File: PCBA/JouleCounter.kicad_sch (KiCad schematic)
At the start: 1 part, among them J101 JTAG

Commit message: Rough outline
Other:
- sheet Main MCU ports: added ~{RESET}; removed none
- sheet UI ports: added INT, SCL, SDA, ~{LCD Reset}; removed none

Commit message: More rough placement
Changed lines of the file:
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@@
+    (effects (font (size 1.27 1.27)) (justify left bottom))
+  )
+  (label "SENSE_USB_D+" (at 76.2 71.12 0)
     (effects (font (size 1.27 1.27)) (justify left bottom))
   )
@@
     (effects (font (size 1.27 1.27)) (justify left bottom))
   )
-  (label "VBus ADC" (at 76.2 93.98 0)
+  (label "VBus ADC" (at 76.2 91.44 0)
     (effects (font (size 1.27 1.27)) (justify left bottom))
   )
@@
     (effects (font (size 1.27 1.27)) (justify left bottom))
   )
+  (label "SENSE_USB_D-" (at 76.2 86.36 0)
+    (effects (font (size 1.27 1.27)) (justify left bottom))
+  )
   (label "I Sense 2" (at 254 69.85 180)
     (effects (font (size 1.27 1.27)) (justify right bottom))
@@
     (effects (font (size 1.27 1.27)) (justify left bottom))
   )
-  (label "USB D- DAC{slash}ADC" (at 76.2 86.36 0)
-    (effects (font (size 1.27 1.27)) (justify left bottom))
-  )
   (label "Spare GPIO 1" (at 76.2 96.52 0)
     (effects (font (size 1.27 1.27)) (justify left bottom))
@@
     (effects (font (size 1.27 1.27)) (justify left bottom))
   )
-  (label "USB D- DAC{slash}ADC" (at 76.2 88.9 0)
-    (effects (font (size 1.27 1.27)) (justify left bottom))
-  )
   (label "JTAG TDO" (at 76.2 121.92 0)
     (effects (font (size 1.27 1.27)) (justify left bottom))
   )
-  (label "Current ADC" (at 76.2 91.44 0)
+  (label "Current ADC" (at 76.2 93.98 0)
     (effects (font (size 1.27 1.27)) (justify left bottom))
   )
@@
     (effects (font (size 1.27 1.27)) (justify left bottom))
   )
-  (label "SENSE_USB_D-" (at 76.2 73.66 0)
+  (label "SENSE_USB_D-" (at 76.2 88.9 0)
     (effects (font (size 1.27 1.27)) (justify left bottom))
   )
@@
     (effects (font (size 1.27 1.27)) (justify left bottom))
   )
-  (label "SENSE_USB_D+" (at 76.2 71.12 0)
-    (effects (font (size 1.27 1.27)) (justify left bottom))
-  )
   (label "Uart Rx" (at 254 116.84 180)
     (effects (font (size 1.27 1.27)) (justify right bottom))
@@
   )
   (label "JTAG TDI" (at 69.85 186.69 0)
+    (effects (font (size 1.27 1.27)) (justify left bottom))
+  )
+  (label "SENSE_USB_D+" (at 76.2 73.66 0)
     (effects (font (size 1.27 1.27)) (justify left bottom))
   )
@@
     )
     (path "/4847c8c0-6173-45c5-9b4b-8c9418cb5a91/3110ff89-db45-4c2b-ae20-9f45ed5b62f3"
-      (reference "L201") (unit 1) (value "2.2uH") (footprint "Inductor_SMD:L_Wuerth_MAPI-3010")
+      (reference "L201") (unit 1) (value "2.2uH") (footprint "Inductor_SMD:L_0805_2012Metric")
     )
     (path "/3f787304-0f09-428f-9615-a178d53b5ed2/eecc54f1-353d-4bbc-bb3a-293df7de7d03/d1c7fa2b-6f66-447f-ab0d-f943727d6017"

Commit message: Routing
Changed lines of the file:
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@@
     (effects (font (size 1.27 1.27)) (justify left bottom))
   )
-  (label "Spare GPIO 1" (at 76.2 96.52 0)
+  (label "Spare GPIO 1" (at 76.2 119.38 0)
     (effects (font (size 1.27 1.27)) (justify left bottom))
   )
@@
     (effects (font (size 1.27 1.27)) (justify right bottom))
   )
-  (label "LCD DC" (at 76.2 109.22 0)
+  (label "LCD DC" (at 76.2 96.52 0)
     (effects (font (size 1.27 1.27)) (justify left bottom))
   )
@@
     (effects (font (size 1.27 1.27)) (justify left bottom))
   )
-  (label "~{TOUCH_IRQ}" (at 76.2 119.38 0)
+  (label "~{TOUCH_IRQ}" (at 76.2 109.22 0)
     (effects (font (size 1.27 1.27)) (justify left bottom))
   )
@@
       (reference "C909") (unit 1) (value "0.1u") (footprint "Capacitor_SMD:C_0603_1608Metric")
     )
-    (path "/61f092db-d732-44e6-ab5b-e56a273f9e01/f833cedb-fa6c-45d4-8bc9-06cb22231f00"
-      (reference "C910") (unit 1) (value "0.1u") (footprint "Capacitor_SMD:C_0603_1608Metric")
-    )
     (path "/61f092db-d732-44e6-ab5b-e56a273f9e01/861d8f10-f76f-4f14-9f74-e11cce68fcd9"
       (reference "C911") (unit 1) (value "1uf") (footprint "Capacitor_SMD:C_0603_1608Metric")
@@
     )
     (path "/3f787304-0f09-428f-9615-a178d53b5ed2/8a06555e-37b5-4e52-aed5-4db5d56c9572/01a2bdc6-039f-41f7-b045-94d753ea8bb9"
-      (reference "L1001") (unit 1) (value "47uH") (footprint "Inductor_SMD:L_Taiyo-Yuden_NR-40xx_HandSoldering")
+      (reference "L1001") (unit 1) (value "47uH") (footprint "Inductor_SMD:L_1210_3225Metric")
     )
     (path "/61f092db-d732-44e6-ab5b-e56a273f9e01/3dcb82af-5522-4234-9097-cffd473db105"

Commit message: molex model
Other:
- sheet ADC Measurements ports: added SCL, SDA, Vsense+, Vsense-, ~{ALERT}; removed ADC Current, ADC VBus, I Sense 1, I Sense 2, VBus In
- note added: "These are doubled up for ADC + DAC operation"
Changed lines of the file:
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@@
   (junction (at 57.15 186.69) (diameter 0) (color 0 0 0 0)
+  )
+  (polyline (pts (xy 88.9 83.82) (xy 91.44 83.82))
+    (stroke (width 0) (type default) (color 0 0 0 0))
   )
   (polyline (pts (xy 228.6 12.7) (xy 228.6 166.37))
@@
     (stroke (width 0) (type default) (color 0 0 0 0))
   )
+  (polyline (pts (xy 88.9 88.9) (xy 91.44 88.9))
+    (stroke (width 0) (type default) (color 0 0 0 0))
+  )
   (wire (pts (xy 57.15 181.61) (xy 57.15 184.15))
     (stroke (width 0) (type default) (color 0 0 0 0))
@@
     (stroke (width 0) (type default) (color 0 0 0 0))
   )
+  (polyline (pts (xy 91.44 68.58) (xy 91.44 73.66))
+    (stroke (width 0) (type default) (color 0 0 0 0))
+  )
   (wire (pts (xy 57.15 186.69) (xy 57.15 189.23))
     (stroke (width 0) (type default) (color 0 0 0 0))
   )
+  (polyline (pts (xy 88.9 68.58) (xy 91.44 68.58))
+    (stroke (width 0) (type default) (color 0 0 0 0))
+  )
+  (polyline (pts (xy 91.44 73.66) (xy 96.52 73.66))
+    (stroke (width 0) (type default) (color 0 0 0 0))
+  )
+  (polyline (pts (xy 88.9 73.66) (xy 91.44 73.66))
+    (stroke (width 0) (type default) (color 0 0 0 0))
+  )
+  (polyline (pts (xy 91.44 83.82) (xy 91.44 88.9))
+    (stroke (width 0) (type default) (color 0 0 0 0))
+  )
   (wire (pts (xy 57.15 184.15) (xy 57.15 186.69))
     (stroke (width 0) (type default) (color 0 0 0 0))
   )
+  (polyline (pts (xy 96.52 83.82) (xy 96.52 73.66))
+    (stroke (width 0) (type default) (color 0 0 0 0))
+  )
   (polyline (pts (xy 171.45 166.37) (xy 176.53 166.37))
+    (stroke (width 0) (type default) (color 0 0 0 0))
+  )
+  (polyline (pts (xy 91.44 83.82) (xy 96.52 83.82))
     (stroke (width 0) (type default) (color 0 0 0 0))
   )
@@
     (effects (font (size 1.27 1.27)) (justify left bottom))
   )
+  (text "These are doubled up for ADC + DAC operation" (at 97.79 77.47 0)
+    (effects (font (size 1.27 1.27)) (justify left bottom))
+  )
   (text "User Interface" (at 185.42 114.3 0)
     (effects (font (size 3 3)) (justify left bottom))
@@
     (effects (font (size 1.27 1.27)) (justify right bottom))
   )
-  (label "Spare GPIO 0" (at 76.2 83.82 0)
+  (label "Spare GPIO 0" (at 76.2 93.98 0)
     (effects (font (size 1.27 1.27)) (justify left bottom))
   )
@@
     (effects (font (size 1.27 1.27)) (justify left bottom))
   )
+  (label "5V_USB" (at 213.36 58.42 0)
+    (effects (font (size 1.27 1.27)) (justify left bottom))
+  )
   (label "~{Reset}" (at 76.2 34.29 0)
     (effects (font (size 1.27 1.27)) (justify left bottom))
@@
     (effects (font (size 1.27 1.27)) (justify right bottom))
   )
+  (label "~{ADC IRQ}" (at 76.2 91.44 0)
+    (effects (font (size 1.27 1.27)) (justify left bottom))
+  )
   (label "LCD SCK" (at 76.2 101.6 0)
     (effects (font (size 1.27 1.27)) (justify left bottom))
@@
     (effects (font (size 1.27 1.27)) (justify left bottom))
   )
-  (label "VBus ADC" (at 76.2 91.44 0)
-    (effects (font (size 1.27 1.27)) (justify left bottom))
-  )
-  (label "VBus" (at 215.9 78.74 0)
-    (effects (font (size 1.27 1.27)) (justify left bottom))
-  )
   (label "JTAG TDI" (at 76.2 45.72 0)
     (effects (font (size 1.27 1.27)) (justify left bottom))
@@
     (effects (font (size 1.27 1.27)) (justify left bottom))
   )
+  (label "~{ADC IRQ}" (at 190.5 83.82 180)
+    (effects (font (size 1.27 1.27)) (justify right bottom))
+  )
   (label "SENSE_USB_D+" (at 254 83.82 180)
     (effects (font (size 1.27 1.27)) (justify right bottom))
@@
     (effects (font (size 1.27 1.27)) (justify left bottom))
   )
+  (label "SDA" (at 190.5 78.74 180)
+    (effects (font (size 1.27 1.27)) (justify right bottom))
+  )
   (label "JTAG TCK" (at 69.85 181.61 0)
     (effects (font (size 1.27 1.27)) (justify left bottom))
@@
     (effects (font (size 1.27 1.27)) (justify left bottom))
   )
-  (label "Current ADC" (at 76.2 93.98 0)
-    (effects (font (size 1.27 1.27)) (justify left bottom))
-  )
   (label "~{TOUCH_IRQ}" (at 76.2 109.22 0)
     (effects (font (size 1.27 1.27)) (justify left bottom))
@@
     (effects (font (size 1.27 1.27)) (justify right bottom))
   )
+  (label "SCL" (at 190.5 81.28 180)
+    (effects (font (size 1.27 1.27)) (justify right bottom))
+  )
   (label "SCL" (at 76.2 78.74 0)
     (effects (font (size 1.27 1.27)) (justify left bottom))
   )
+  (label "5V_USB" (at 213.36 36.83 0)
+    (effects (font (size 1.27 1.27)) (justify left bottom))
+  )
   (label "SDA" (at 215.9 142.24 0)
     (effects (font (size 1.27 1.27)) (justify left bottom))
   )
-  (label "VBus ADC" (at 190.5 78.74 180)
-    (effects (font (size 1.27 1.27)) (justify right bottom))
-  )
   (label "CC2_X" (at 213.36 54.61 0)
     (effects (font (size 1.27 1.27)) (justify left bottom))
@@
   )
   (label "SDA" (at 254 119.38 180)
-    (effects (font (size 1.27 1.27)) (justify right bottom))
-  )
-  (label "Current ADC" (at 190.5 85.09 180)
     (effects (font (size 1.27 1.27)) (justify right bottom))
   )
@@
       (effects (font (size 1.27 1.27)) (justify left top))
     )
-    (pin "VBus In" input (at 215.9 78.74 0)
-      (effects (font (size 1.27 1.27)) (justify right))
-    )
-    (pin "I Sense 1" input (at 215.9 81.28 0)
-      (effects (font (size 1.27 1.27)) (justify right))
-    )
-    (pin "I Sense 2" input (at 215.9 83.82 0)
-      (effects (font (size 1.27 1.27)) (justify right))
-    )
-    (pin "ADC VBus" input (at 190.5 78.74 180)
-      (effects (font (size 1.27 1.27)) (justify left))
-    )
-    (pin "ADC Current" input (at 190.5 85.09 180)
+    (pin "SDA" input (at 190.5 78.74 180)
+      (effects (font (size 1.27 1.27)) (justify left))
+    )
+    (pin "SCL" input (at 190.5 81.28 180)
+      (effects (font (size 1.27 1.27)) (justify left))
+    )
+    (pin "Vsense+" input (at 215.9 81.28 0)
+      (effects (font (size 1.27 1.27)) (justify right))
+    )
+    (pin "Vsense-" input (at 215.9 83.82 0)
+      (effects (font (size 1.27 1.27)) (justify right))
+    )
+    (pin "~{ALERT}" input (at 190.5 83.82 180)
       (effects (font (size 1.27 1.27)) (justify left))
     )
@@
       (reference "#PWR0133") (unit 1) (value "GND") (footprint "")
     )
+    (path "/22f53838-7224-4d50-99f8-44746cd87af7/70cfc3de-356f-422f-8660-4b73d4360b3f"
+      (reference "#PWR0134") (unit 1) (value "VDD") (footprint "")
+    )
+    (path "/22f53838-7224-4d50-99f8-44746cd87af7/49693641-4499-473f-b005-4324d8fa543f"
+      (reference "#PWR0135") (unit 1) (value "GND") (footprint "")
+    )
     (path "/b0bcfef4-b206-452e-922a-e4174969def9/42d40598-f1c5-4992-939b-06617e7a59a8"
       (reference "#PWR0136") (unit 1) (value "GND") (footprint "")
@@
       (reference "#PWR0138") (unit 1) (value "GND") (footprint "")
     )
-    (path "/22f53838-7224-4d50-99f8-44746cd87af7/6a14883c-e23a-4bd5-84e9-8efebed799c9"
-      (reference "#PWR0139") (unit 1) (value "GND") (footprint "")
-    )
-    (path "/22f53838-7224-4d50-99f8-44746cd87af7/2116ac8a-6c19-4db6-aec1-63bf7b161e34"
-      (reference "#PWR0140") (unit 1) (value "VDD") (footprint "")
-    )
-    (path "/22f53838-7224-4d50-99f8-44746cd87af7/63d18546-978a-4ade-b5df-12f3cfd04a15"
-      (reference "#PWR0141") (unit 1) (value "GND") (footprint "")
-    )
-    (path "/22f53838-7224-4d50-99f8-44746cd87af7/c78b9413-d043-4274-8cdb-66dcb9cc5a63"
-      (reference "#PWR0142") (unit 1) (value "VDD") (footprint "")
-    )
-    (path "/22f53838-7224-4d50-99f8-44746cd87af7/0d93a723-51a6-484f-9d01-65584e9aaa36"
-      (reference "#PWR0143") (unit 1) (value "GND") (footprint "")
-    )
     (path "/61f092db-d732-44e6-ab5b-e56a273f9e01/b98ff10d-591f-4fd6-bc6c-5200de8ff75b"
       (reference "#PWR0144") (unit 1) (value "VDD") (footprint "")
@@
       (reference "C906") (unit 1) (value "4.7uF") (footprint "Capacitor_SMD:C_0603_1608Metric")
     )
-    (path "/61f092db-d732-44e6-ab5b-e56a273f9e01/4ddcb3be-e691-47ab-8d2c-2a86dcf18c28"
-      (reference "C907") (unit 1) (value "C") (footprint "Capacitor_SMD:C_0603_1608Metric")
-    )
     (path "/61f092db-d732-44e6-ab5b-e56a273f9e01/ef8e7170-b57e-43ee-8ecc-246fb9cca5af"
       (reference "C908") (unit 1) (value "0.1u") (footprint "Capacitor_SMD:C_0603_1608Metric")
@@
       (reference "R602") (unit 1) (value "5.1k") (footprint "Resistor_SMD:R_0603_1608Metric")
     )
-    (path "/22f53838-7224-4d50-99f8-44746cd87af7/e02c9cd3-fe72-4738-8106-3699abc57d7d"
-      (reference "R701") (unit 1) (value "1.4M") (footprint "Resistor_SMD:R_0603_1608Metric")
-    )
-    (path "/22f53838-7224-4d50-99f8-44746cd87af7/2d505387-6c15-4319-ab31-315284aa4c23"
-      (reference "R702") (unit 1) (value "100K") (footprint "Resistor_SMD:R_0603_1608Metric")
-    )
-    (path "/22f53838-7224-4d50-99f8-44746cd87af7/d44ca519-5ef2-4374-a2c3-7acf0f68ff9a"
-      (reference "R703") (unit 1) (value "100K") (footprint "Resistor_SMD:R_0603_1608Metric")
-    )
-    (path "/22f53838-7224-4d50-99f8-44746cd87af7/456f46ba-2422-4e6e-930f-9ba6750d29da"
-      (reference "R704") (unit 1) (value "100K") (footprint "Resistor_SMD:R_0603_1608Metric")
-    )
     (path "/3f787304-0f09-428f-9615-a178d53b5ed2/eecc54f1-353d-4bbc-bb3a-293df7de7d03/b92138fa-003e-47d5-b5d1-647201a1e7dc"
       (reference "R901") (unit 1) (value "200k") (footprint "Resistor_SMD:R_0603_1608Metric")
@@
       (reference "U401") (unit 1) (value "FUSB302B") (footprint "Package_DFN_QFN:WQFN-14-1EP_2.5x2.5mm_P0.5mm_EP1.45x1.45mm")
     )
-    (path "/22f53838-7224-4d50-99f8-44746cd87af7/df2400cd-5435-4261-addb-51b872c3b57c"
-      (reference "U701") (unit 1) (value "INA181") (footprint "Package_TO_SOT_SMD:SOT-23-6")
+    (path "/22f53838-7224-4d50-99f8-44746cd87af7/7661659d-bd7d-4ade-8c3b-3e6c0b2a79c1"
+      (reference "U701") (unit 1) (value "INA226") (footprint "Package_SO:VSSOP-10_3x3mm_P0.5mm")
     )
     (path "/3f787304-0f09-428f-9615-a178d53b5ed2/1e50f7c6-3080-4467-aaf5-2bf00cdf949f"

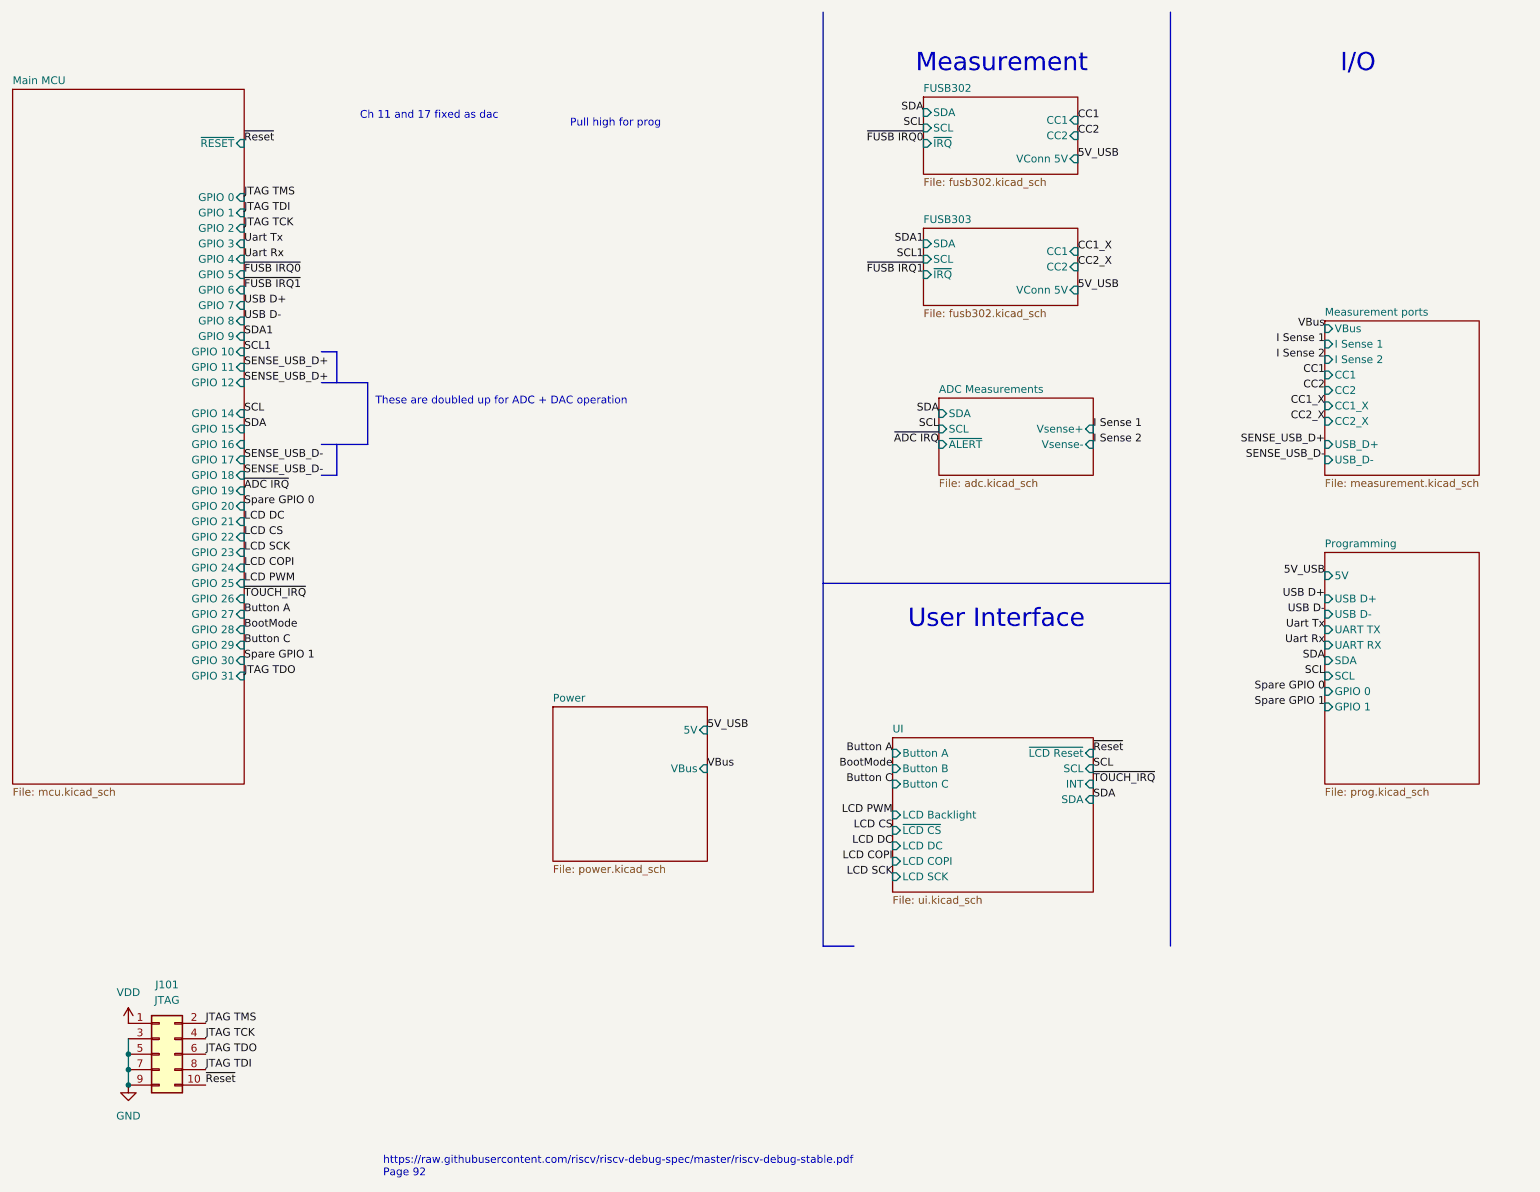
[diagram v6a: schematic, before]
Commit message: Jtag on usb-c
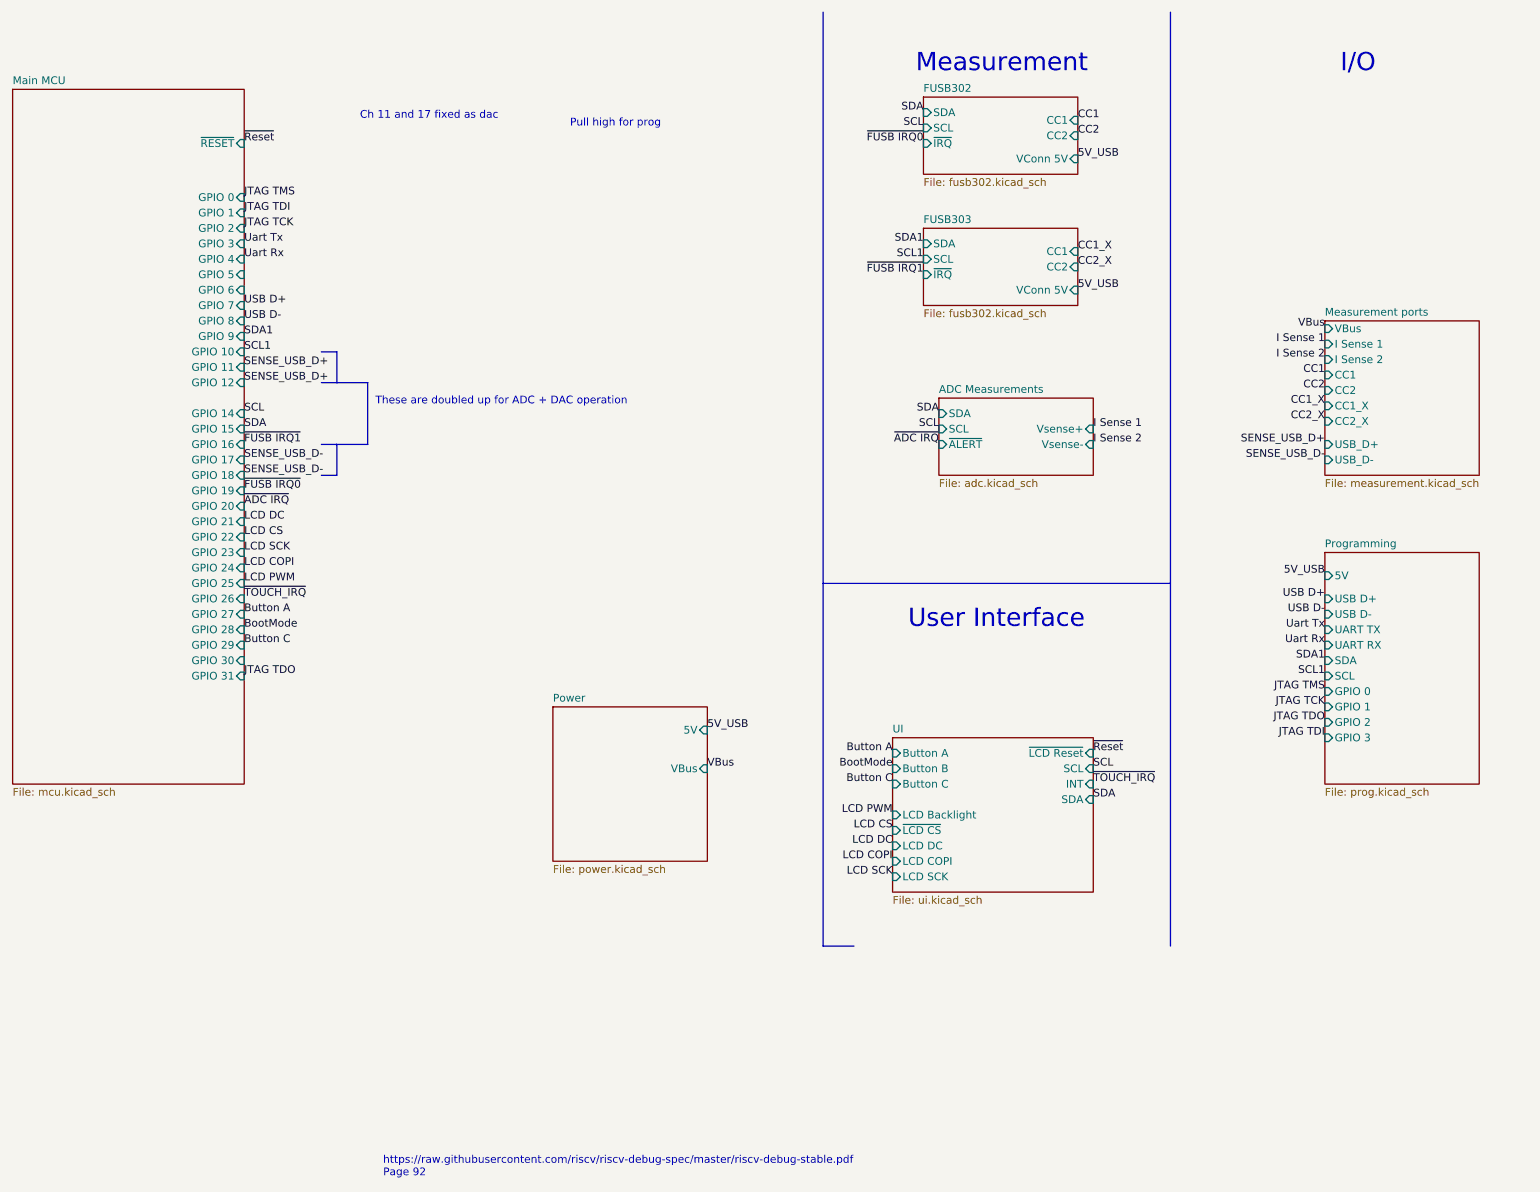
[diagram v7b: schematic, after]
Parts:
- removed J101: JTAG, Connector_PinHeader_2.54mm:PinHeader_2x05_P2.54mm_Vertical, symbol Connector_Generic:Conn_02x05_Odd_Even
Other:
- sheet Programming ports: added GPIO 2, GPIO 3; removed none
